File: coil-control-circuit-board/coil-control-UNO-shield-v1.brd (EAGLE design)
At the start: 54.6 x 59.7 mm, 26 parts, among them Q1 IRLML0060, Q2 IRLML0060, SW2 BUTTON, SW3 BUTTON, U2 LM4250, U3 LM4250

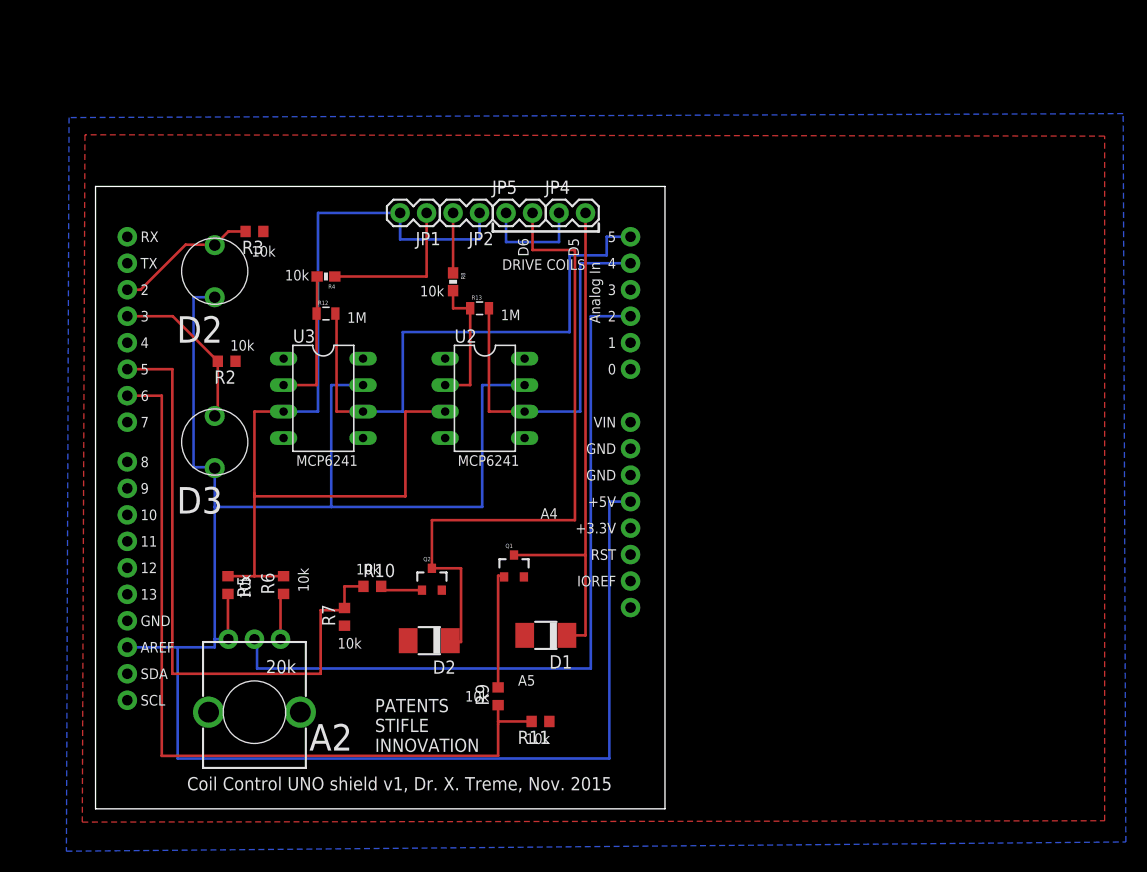
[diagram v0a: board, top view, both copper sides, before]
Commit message: finished the boards, mostly
added DC power connector, shifted everything over to work on the Yun(
make space for the big connectors), connected Vin to the input DC
power, cleaned stuff up a bit, moved stuff around.
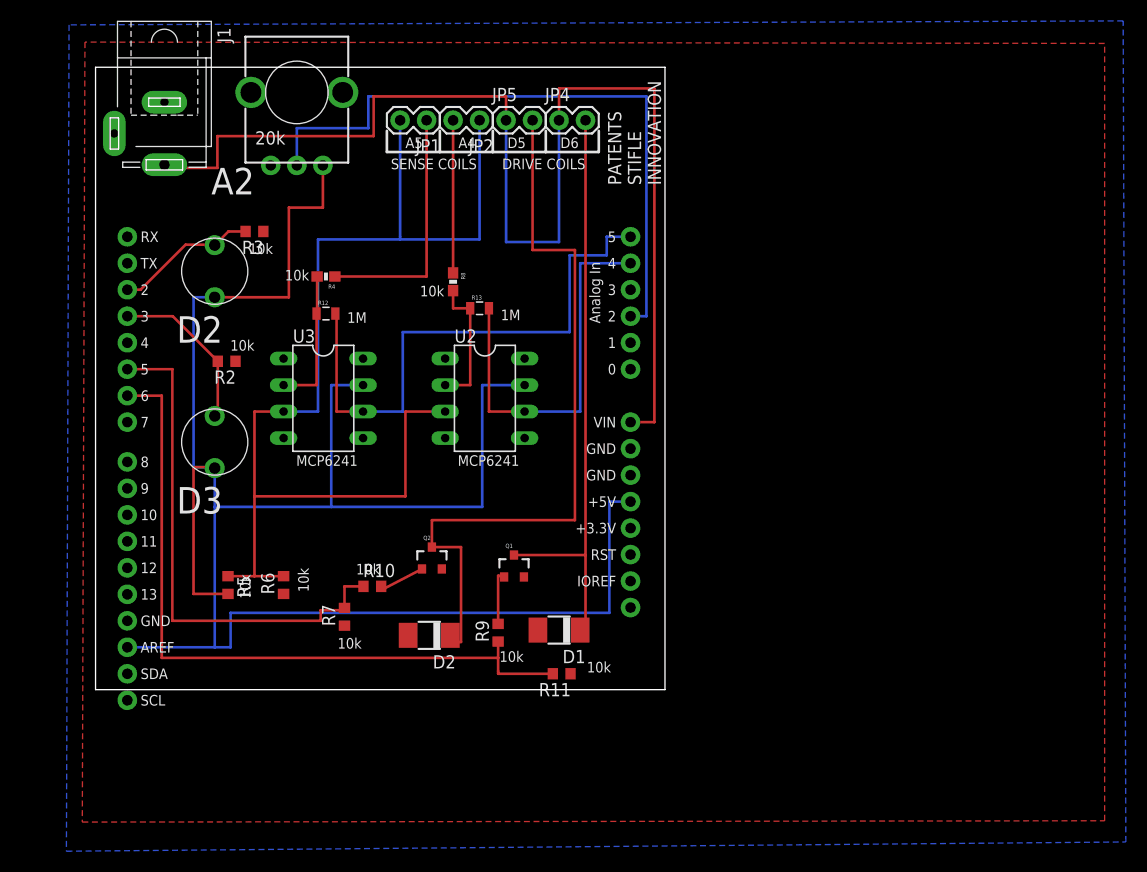
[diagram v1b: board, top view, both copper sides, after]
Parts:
- added J1: (no value), con-jack:SPC4078
- moved R15 59.6 mm to (19.3, 68.7), turned to 270 degrees
- moved JP1 8.89 mm to (31.8, 66.0)
- moved JP2 8.89 mm to (36.8, 66.0)
- moved JP4 8.89 mm to (44.5, 66.0)
- moved JP5 8.89 mm to (39.4, 66.0)
- moved R9 6.10 mm to (38.6, 16.9)
- moved R11 5.00 mm to (44.7, 13.0)
- moved Q2 2.03 mm to (32.3, 24.0)
- moved D1 1.37 mm to (44.5, 17.1)
- moved D2 0.51 mm to (32.0, 16.6)
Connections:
- net GND: now also J1.1, J1.2
- net VPOWER: now also J1.3, U$1.VIN
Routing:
- net VPOWER: track 10.7 -> 117.1 mm
- net MIDV: track 93.3 -> 108.5 mm
- net D5: track 60.2 -> 50.1 mm
- net VCC: track 186.6 -> 196.6 mm
- net A2: track 72.7 -> 62.8 mm
- net N$18: track 62.9 -> 72.3 mm
- net D6: track 78.2 -> 69.0 mm
- net SENSECOIL2: track 14.9 -> 23.8 mm
- net SENSECOIL: track 5.75 -> 14.6 mm
- net N$15: track 49.2 -> 57.0 mm
- net N$13: track 11.4 -> 5.30 mm
- net GND: track 4.64 -> 0.00 mm
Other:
- board text added: "SENSE COILS"
- board text removed: "Coil Control UNO shield v1, Dr. X. Treme, Nov. 2015"

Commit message: added BOM for shield board
and also tweaked board file a bit
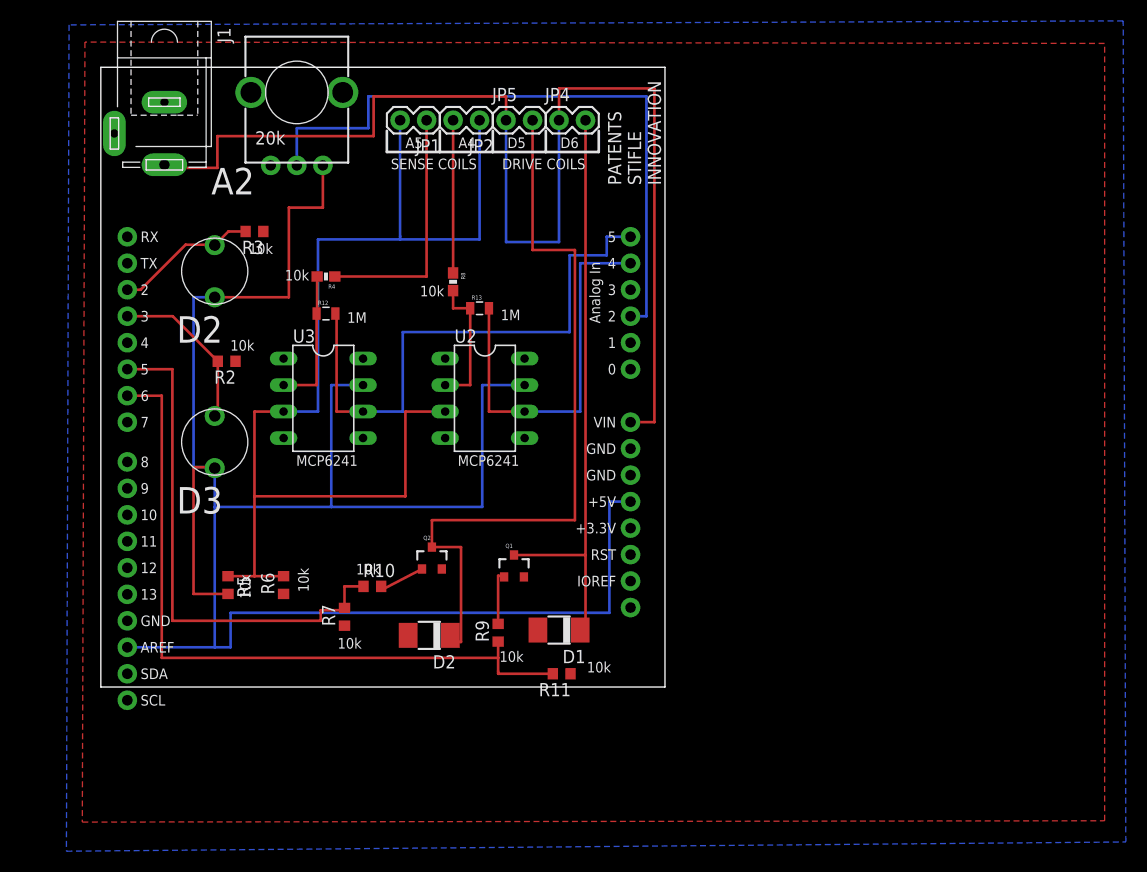
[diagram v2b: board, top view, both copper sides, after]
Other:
- board size 54.6 x 59.7 mm -> 54.1 x 59.4 mm
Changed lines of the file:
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@@
 <board>
 <plain>
-<wire x1="0" y1="11.43" x2="54.61" y2="11.43" width="0" layer="20"/>
-<wire x1="54.61" y1="11.43" x2="54.61" y2="71.12" width="0" layer="20"/>
-<wire x1="54.61" y1="71.12" x2="0" y2="71.12" width="0" layer="20"/>
-<wire x1="0" y1="71.12" x2="0" y2="11.43" width="0" layer="20"/>
+<wire x1="0.508" y1="11.684" x2="54.61" y2="11.684" width="0" layer="20"/>
+<wire x1="54.61" y1="11.684" x2="54.61" y2="71.12" width="0" layer="20"/>
+<wire x1="54.61" y1="71.12" x2="0.508" y2="71.12" width="0" layer="20"/>
+<wire x1="0.508" y1="71.12" x2="0.508" y2="11.684" width="0" layer="20"/>
 <text x="54.229" y="59.817" size="1.27" layer="21" rot="SR90">PATENTS
 STIFLE
